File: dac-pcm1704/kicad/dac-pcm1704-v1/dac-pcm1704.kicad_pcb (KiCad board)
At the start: 4 copper layers, 76.2 x 53.3 mm, 81 parts, among them IC2 PCM1702P, IC3 PCM1704U, J10 GND, J11 +15VAIN, J12 GND, J13 -15VAIN, J15 A, J16 +5VIN, J17 GND, J18 GND, J2 Conn_02x07_Odd_Even, J3 +5VAIN, J6 OUT, J7 -5VAIN, J8 GND, J9 OUT, U1 OPA1612, U2 TC1185-1.8VCT713, U3 TC1185-3.3VCT713, U4 XC2C64A-xVQ44, U5 CM1293A−04SO, U6 OPA1612

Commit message: WIP
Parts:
- removed IC2: PCM1702P, Package_DIP:DIP-16_W7.62mm
- added IC4: PCM1704U, Package_SO:SO-20_5.3x12.6mm_P1.27mm, F.Cu at (149.3, 99.5)
- C11, C12, C20, C21, C26: moved to B.Cu
- C25: footprint Capacitor_Tantalum_SMD:CP_EIA-3216-18_Kemet-A_Pad1.58x1.35mm_HandSolder -> Capacitor_SMD:C_1206_3216Metric_Pad1.33x1.80mm_HandSolder; moved to B.Cu
- C27, C28, C30: footprint Capacitor_Tantalum_SMD:CP_EIA-3216-18_Kemet-A_Pad1.58x1.35mm_HandSolder -> Capacitor_SMD:C_1206_3216Metric_Pad1.33x1.80mm_HandSolder
- C35, C36: footprint Capacitor_Tantalum_SMD:CP_EIA-3528-21_Kemet-B_Pad1.50x2.35mm_HandSolder -> Capacitor_SMD:C_1206_3216Metric_Pad1.33x1.80mm_HandSolder
- moved C11 33.3 mm to (149.0, 73.9), turned to 180 degrees
- moved C12 33.2 mm to (149.0, 71.3), turned to 180 degrees
- moved C16 31.6 mm to (154.4, 86.0)
- moved C10 31.2 mm to (156.6, 80.2)
- moved C29 31.2 mm to (141.4, 72.5)
- moved C14 31.2 mm to (143.5, 77.0)
- moved C9 31.2 mm to (153.8, 83.3)
- moved IC3 31.2 mm to (149.3, 75.7)
- moved C18 31.2 mm to (141.4, 77.6)
- moved C15 31.2 mm to (143.5, 73.2)
- moved C13 30.9 mm to (153.8, 68.1), turned to 0 degrees
- moved C17 30.6 mm to (154.3, 65.9), turned to 180 degrees
- moved C25 12.4 mm to (150.4, 101.7), turned to -90 degrees
- moved C26 8.43 mm to (148.2, 101.2), turned to -90 degrees
- moved C20 8.42 mm to (148.7, 97.6), turned to 180 degrees
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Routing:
- net +5VA: track 20.1 -> 54.4 mm, vias 0 -> 1
- net -5VA: track 36.2 -> 58.9 mm
- net DATAOUTL: track 2.86 -> 16.9 mm, vias 1 -> 2
- net GND: track 17.1 -> 28.3 mm, vias 0 -> 4
- net Net-(IC4-IOUT): track 15.2 -> 4.62 mm, vias 1 -> 0
- net CLKOUTL: track 12.5 -> 17.0 mm, vias 1 -> 2
- net LEOUTL: track 21.8 -> 22.6 mm, vias 1 -> 2
- net Net-(IC4-SERV_DC): track 2.35 -> 2.46 mm, vias 0 -> 1
- net Net-(IC4-REF_DC): track 2.35 -> 2.46 mm, vias 0 -> 1

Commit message: WIP
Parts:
- C14, C18: moved to B.Cu
- moved C18 9.16 mm to (150.4, 76.3), turned to -90 degrees
- moved C14 4.81 mm to (148.2, 75.8), turned to -90 degrees
- moved C19 2.39 mm to (156.6, 101.5)
- moved C21 2.39 mm to (148.7, 92.7)
- moved C22 2.39 mm to (143.6, 96.2)
- moved C23 2.39 mm to (153.8, 104.7)
- moved C25 2.39 mm to (150.4, 99.3)
- moved C30 2.39 mm to (154.3, 86.9)
- moved C20 2.39 mm to (148.7, 95.2)
- moved C24 2.39 mm to (153.8, 89.5)
- moved C26 2.39 mm to (148.2, 98.8)
- moved C27 2.39 mm to (141.4, 96.8)
- moved IC4 2.39 mm to (149.3, 97.1)
- moved C28 1.98 mm to (154.4, 107.4)
- moved C17 1.88 mm to (154.3, 64.1)
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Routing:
- net +5VA: track 54.4 -> 38.3 mm, vias 1 -> 0
- net LEOUTL: track 22.6 -> 6.68 mm, vias 2 -> 1
- net GND: track 28.3 -> 17.1 mm, vias 4 -> 0
- net CLKOUTL: track 17.0 -> 7.43 mm, vias 2 -> 1
- net DATAOUTL: track 16.9 -> 8.03 mm, vias 2 -> 1
- net -5VA: track 58.9 -> 63.8 mm, vias 1 -> 2
- net Net-(IC4-SERV_DC): track 2.46 -> 0.00 mm, vias 1 -> 0
- net Net-(IC4-REF_DC): track 2.46 -> 0.00 mm, vias 1 -> 0
- net Net-(IC4-BPO_DC): track 2.24 -> 0.00 mm
- net unconnected-(IC4-NC-Pad8): track 0.00 -> 0.60 mm

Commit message: WIP
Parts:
- removed J15: A, kicad-snk:TE_CONN_RCPT_10POS_0.1_TIN_PCB
- added J4: TE MicroMatch, Connector_TE-Connectivity:TE_Micro-MaTch_1-215079-0_2x05_P1.27mm_Vertical, F.Cu at (112.8, 74.6)
- moved C27 1.22 mm to (140.2, 96.8)
- moved C29 0.91 mm to (140.2, 73.7)
- moved C15 0.91 mm to (142.6, 73.2)
- moved C22 0.91 mm to (142.6, 96.2)
- moved C11 0.10 mm to (148.7, 72.2)
- moved C12 0.05 mm to (148.7, 69.6)
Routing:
- net GND: track 17.1 -> 56.1 mm, vias 0 -> 4
- net -5VA: track 63.8 -> 101.1 mm, vias 2 -> 4
- net +5VA: track 38.3 -> 60.5 mm, vias 0 -> 4
- net Net-(IC3-SERV_DC): track 0.00 -> 2.54 mm, vias 0 -> 1
- net Net-(IC3-REF_DC): track 0.00 -> 2.51 mm, vias 0 -> 1
- net Net-(IC4-SERV_DC): track 0.00 -> 2.46 mm, vias 0 -> 1
- net Net-(IC4-REF_DC): track 0.00 -> 2.46 mm, vias 0 -> 1
- net Net-(IC4-BPO_DC): track 0.00 -> 2.24 mm
- net Net-(IC3-BPO_DC): track 0.00 -> 2.24 mm

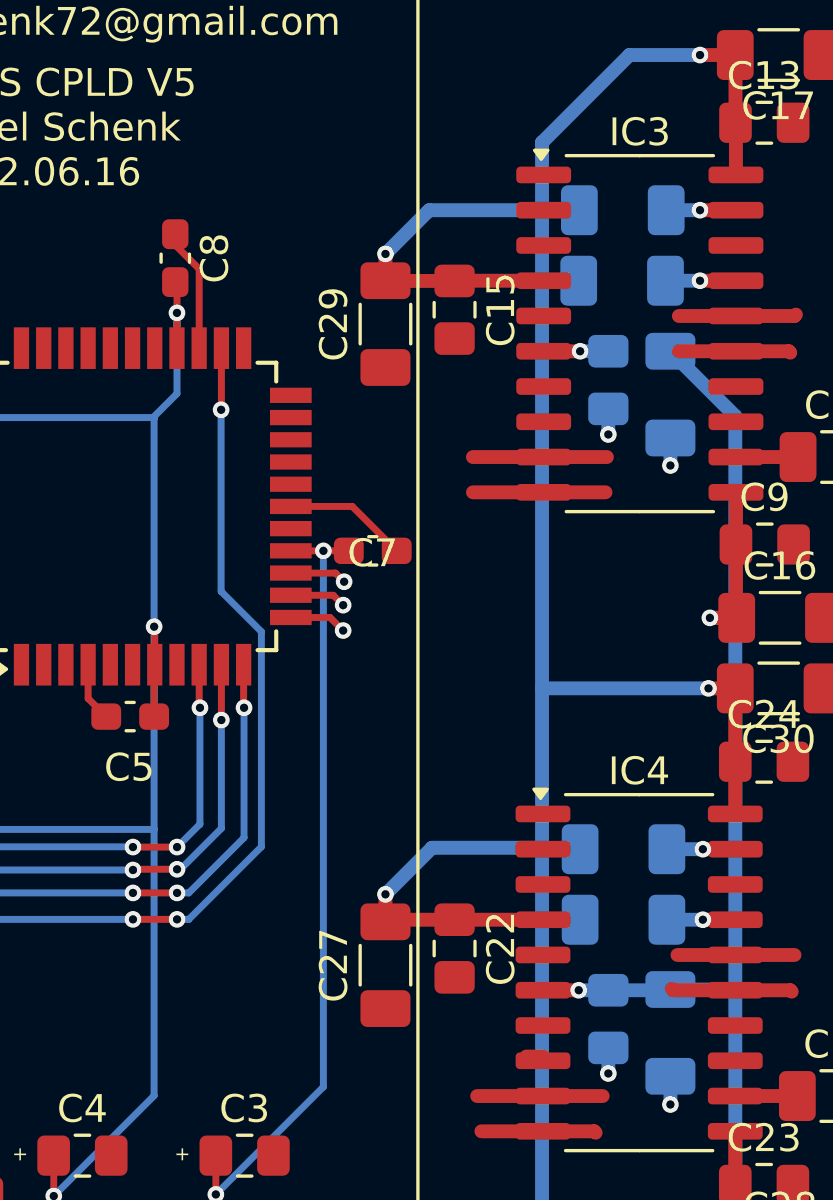
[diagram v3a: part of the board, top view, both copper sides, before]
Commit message: Update dac-pcm1704.kicad_pcb
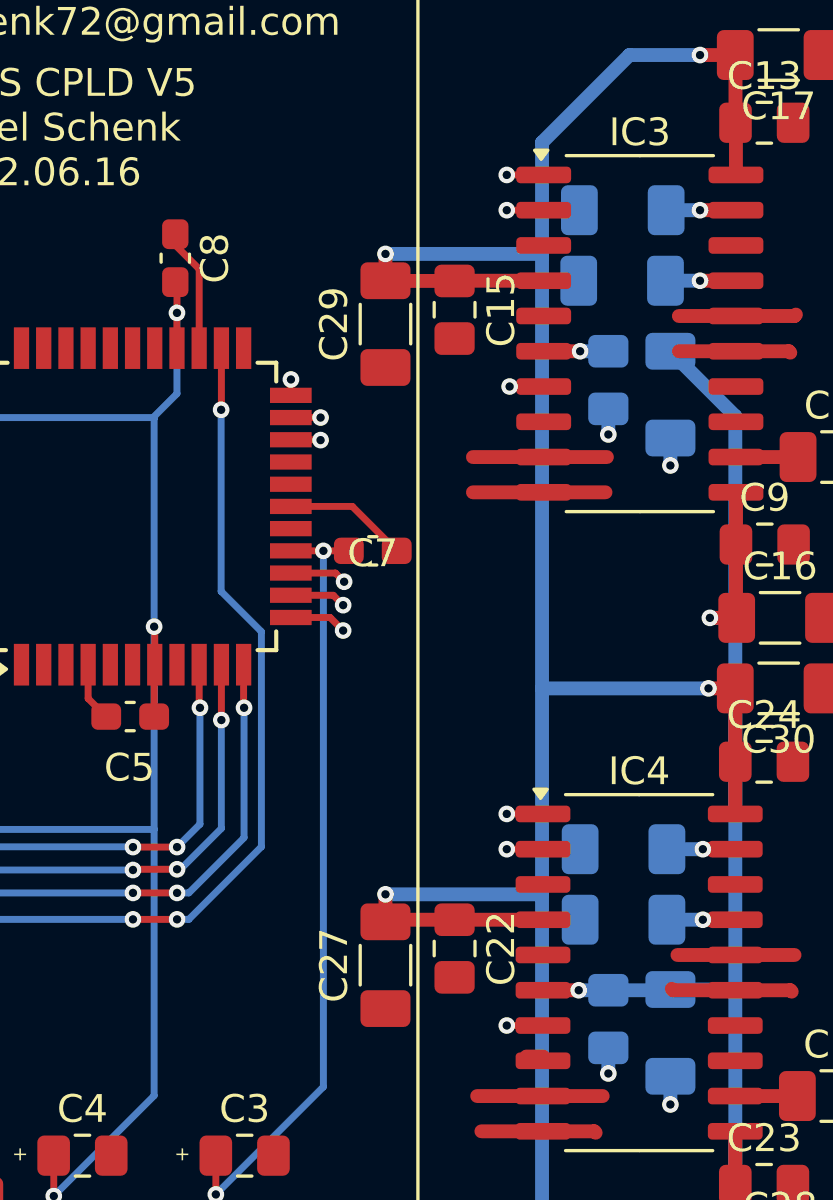
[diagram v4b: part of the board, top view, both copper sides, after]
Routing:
- net DATAOUTR: track 0.00 -> 12.7 mm, vias 0 -> 2
- net CLKOUTR: track 0.00 -> 12.6 mm, vias 0 -> 2
- net LEOUTR: track 0.00 -> 9.91 mm, vias 0 -> 2
- net DATAOUTL: track 8.03 -> 3.36 mm, vias 1 -> 2
- net CLKOUTL: track 7.43 -> 3.34 mm, vias 1 -> 2
- net LEOUTL: track 6.68 -> 3.38 mm, vias 1 -> 2
- net -5VA: track 101.1 -> 99.7 mm
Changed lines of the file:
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@@
+	)
+	(segment
+		(start 136.749 76.315)
+		(end 136.749 75.7474)
+		(width 0.25)
+		(layer "F.Cu")
+		(net 13)
+	)
+	(segment
+		(start 136.749 75.7474)
+		(end 136.7536 75.7428)
+		(width 0.25)
+		(layer "F.Cu")
+		(net 13)
+	)
+	(segment
+		(start 145.8552 68.3768)
+		(end 144.526 68.3768)
+		(width 0.25)
+		(layer "F.Cu")
+		(net 13)
+	)
+	(via
+		(at 144.526 68.3768)
+		(size 0.6)
+		(drill 0.3)
+		(layers "F.Cu" "B.Cu")
+		(net 13)
+	)
+	(via
+		(at 136.7536 75.7428)
+		(size 0.6)
+		(drill 0.3)
+		(layers "F.Cu" "B.Cu")
+		(net 13)
+	)
+	(segment
+		(start 144.526 68.3768)
+		(end 144.1196 68.3768)
+		(width 0.25)
+		(layer "In1.Cu")
+		(net 13)
+	)
+	(segment
+		(start 144.1196 68.3768)
+		(end 136.7536 75.7428)
+		(width 0.25)
+		(layer "In1.Cu")
+		(net 13)
 	)
 	(segment
@@
 	)
 	(segment
+		(start 145.8306 91.3892)
+		(end 144.526 91.3892)
+		(width 0.25)
+		(layer "F.Cu")
+		(net 14)
+	)
+	(segment
 		(start 138.355937 82.715)
 		(end 138.668128 83.027191)
@@
 	)
 	(via
+		(at 144.526 91.3892)
+		(size 0.6)
+		(drill 0.3)
+		(layers "F.Cu" "B.Cu")
+		(net 14)
+	)
+	(via
 		(at 138.668128 83.027191)
 		(size 0.6)
@@
 	)
 	(segment
-		(start 142.9004 87.252702)
-		(end 138.674889 83.027191)
+		(start 138.674889 83.027191)
+		(end 138.668128 83.027191)
 		(width 0.25)
 		(layer "In1.Cu")
@@
 	)
 	(segment
-		(start 138.674889 83.027191)
-		(end 138.668128 83.027191)
-		(width 0.25)
-		(layer "In1.Cu")
-		(net 14)
-	)
-	(segment
 		(start 152.7802 79.8068)
 		(end 152.7802 81.6864)
@@
 	)
 	(segment
-		(start 145.796 92.6084)
+		(start 145.796 94.2848)
 		(end 145.796 95.1484)
 		(width 0.5)
@@
 	)
 	(segment
-		(start 145.796 92.6084)
-		(end 141.8336 92.6084)
-		(width 0.5)
-		(layer "B.Cu")
-		(net 17)
-	)
-	(segment
 		(start 147.1676 95.1992)
 		(end 145.8468 95.1992)
@@
 	)
 	(segment
+		(start 145.796 69.596)
+		(end 145.796 71.3232)
+		(width 0.5)
+		(layer "B.Cu")
+		(net 17)
+	)
+	(segment
 		(start 145.796 95.1484)
 		(end 145.796 108.7755)
@@
 	)
 	(segment
-		(start 141.732 69.6468)
-		(end 140.1572 71.2216)
-		(width 0.5)
-		(layer "B.Cu")
-		(net 17)
-	)
-	(segment
 		(start 151.4856 64.0588)
 		(end 148.9456 64.0588)
@@
 	)
 	(segment
+		(start 140.1572 94.2848)
+		(end 145.796 94.2848)
+		(width 0.5)
+		(layer "B.Cu")
+		(net 17)
+	)
+	(segment
+		(start 145.6944 71.2216)
+		(end 145.796 71.3232)
+		(width 0.5)
+		(layer "B.Cu")
+		(net 17)
+	)
+	(segment
 		(start 147.1168 72.1868)
 		(end 145.796 72.1868)
@@
 	)
 	(segment
-		(start 145.796 69.596)
+		(start 145.796 92.6084)
+		(end 145.796 94.2848)
+		(width 0.5)
+		(layer "B.Cu")
+		(net 17)
+	)
+	(segment
+		(start 140.1572 71.2216)
+		(end 145.6944 71.2216)
+		(width 0.5)
+		(layer "B.Cu")
+		(net 17)
+	)
+	(segment
+		(start 145.796 71.3232)
 		(end 145.796 72.1868)
-		(width 0.5)
-		(layer "B.Cu")
-		(net 17)
-	)
-	(segment
-		(start 141.8336 92.6084)
-		(end 140.1572 94.2848)
-		(width 0.5)
-		(layer "B.Cu")
-		(net 17)
-	)
-	(segment
-		(start 145.8468 69.6468)
-		(end 141.732 69.6468)
 		(width 0.5)
 		(layer "B.Cu")
@@
 	)
 	(segment
+		(start 145.8552 75.9968)
+		(end 144.6276 75.9968)
+		(width 0.25)
+		(layer "F.Cu")
+		(net 22)
+	)
+	(segment
+		(start 136.749 77.915)
+		(end 137.8082 77.915)
+		(width 0.25)
+		(layer "F.Cu")
+		(net 22)
+	)
+	(segment
+		(start 137.8082 77.915)
+		(end 137.8204 77.9272)
+		(width 0.25)
+		(layer "F.Cu")
+		(net 22)
+	)
+	(via
+		(at 144.6276 75.9968)
+		(size 0.6)
+		(drill 0.3)
+		(layers "F.Cu" "B.Cu")
+		(net 22)
+	)
+	(via
+		(at 137.8204 77.9272)
+		(size 0.6)
+		(drill 0.3)
+		(layers "F.Cu" "B.Cu")
+		(net 22)
+	)
+	(segment
+		(start 137.8204 77.9272)
+		(end 139.192 77.9272)
+		(width 0.25)
+		(layer "In1.Cu")
+		(net 22)
+	)
+	(segment
+		(start 141.1224 75.9968)
+		(end 144.6276 75.9968)
+		(width 0.25)
+		(layer "In1.Cu")
+		(net 22)
+	)
+	(segment
+		(start 139.192 77.9272)
+		(end 141.1224 75.9968)
+		(width 0.25)
+		(layer "In1.Cu")
+		(net 22)
+	)
+	(segment
+		(start 137.8198 77.115)
+		(end 137.8204 77.1144)
+		(width 0.25)
+		(layer "F.Cu")
+		(net 23)
+	)
+	(segment
+		(start 136.749 77.115)
+		(end 137.8198 77.115)
+		(width 0.25)
+		(layer "F.Cu")
+		(net 23)
+	)
+	(segment
+		(start 145.8552 69.6468)
+		(end 144.526 69.6468)
+		(width 0.25)
+		(layer "F.Cu")
+		(net 23)
+	)
+	(via
+		(at 144.526 69.6468)
+		(size 0.6)
+		(drill 0.3)
+		(layers "F.Cu" "B.Cu")
+		(net 23)
+	)
+	(via
+		(at 137.8204 77.1144)
+		(size 0.6)
+		(drill 0.3)
+		(layers "F.Cu" "B.Cu")
+		(net 23)
+	)
+	(segment
+		(start 138.7856 75.3872)
+		(end 144.526 69.6468)
+		(width 0.25)
+		(layer "In1.Cu")
+		(net 23)
+	)
+	(segment
+		(start 137.8204 77.1144)
+		(end 138.7856 76.1492)
+		(width 0.25)
+		(layer "In1.Cu")
+		(net 23)
+	)
+	(segment
+		(start 138.7856 76.1492)
+		(end 138.7856 75.3872)
+		(width 0.25)
+		(layer "In1.Cu")
+		(net 23)
+	)
+	(segment
 		(start 136.749 84.315)
 		(end 138.163 84.315)
@@
 		(net 24)
 	)
+	(segment
+		(start 145.8306 99.0092)
+		(end 144.526 99.0092)
+		(width 0.25)
+		(layer "F.Cu")
+		(net 24)
+	)
 	(via
 		(at 138.6332 84.7852)
@@
 		(net 24)
 	)
-	(segment
-		(start 141.8844 88.0364)
-		(end 138.6332 84.7852)
-		(width 0.25)
-		(layer "In1.Cu")
+	(via
+		(at 144.526 99.0092)
+		(size 0.6)
+		(drill 0.3)
+		(layers "F.Cu" "B.Cu")
 		(net 24)
 	)
@@
 	)
 	(segment
+		(start 145.8306 92.6592)
+		(end 144.526 92.6592)
+		(width 0.25)
+		(layer "F.Cu")
+		(net 25)
+	)
+	(segment
 		(start 136.749 83.515)
 		(end 138.2774 83.515)
@@
 		(net 25)
 	)
-	(segment
-		(start 138.6332 83.8708)
-		(end 142.4494 87.687)
-		(width 0.25)
-		(layer "In1.Cu")
+	(via
+		(at 144.526 92.6592)
+		(size 0.6)
+		(drill 0.3)
+		(layers "F.Cu" "B.Cu")
 		(net 25)
 	)

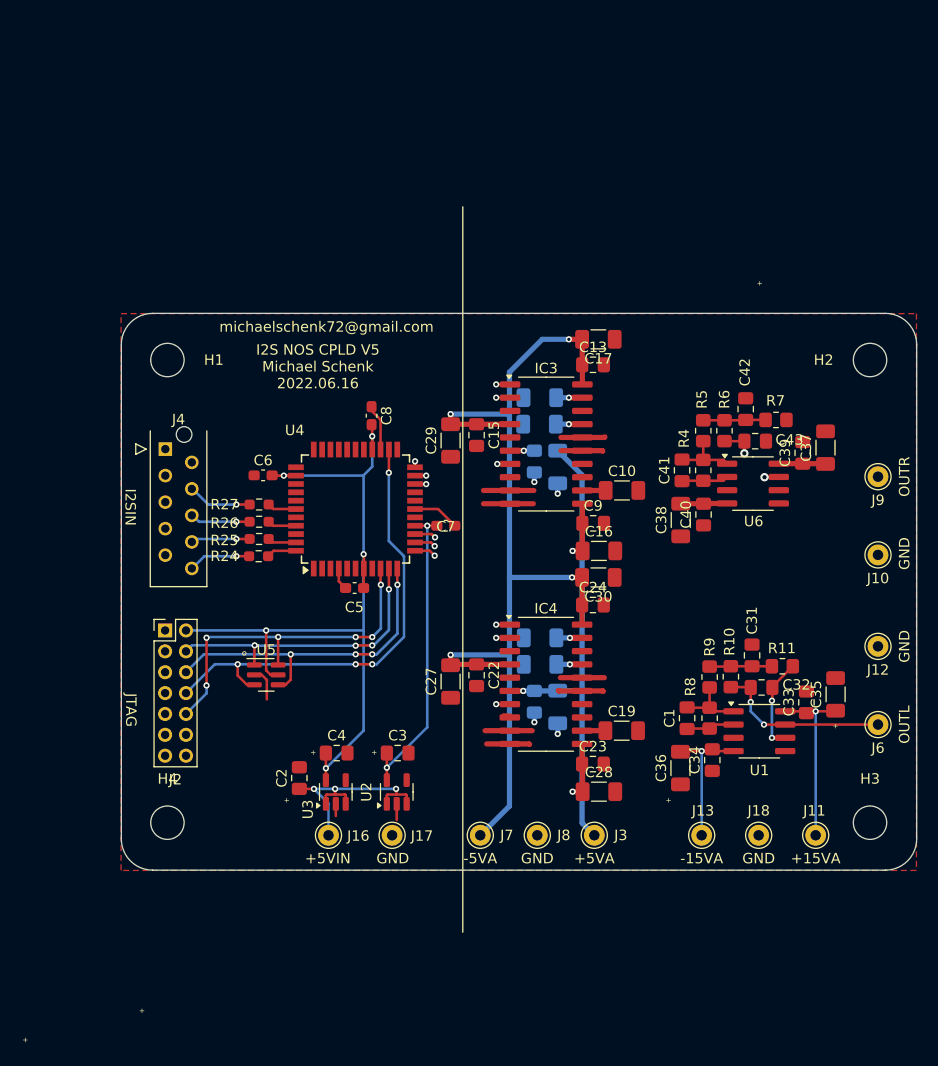
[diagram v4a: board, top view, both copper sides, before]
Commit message: Update dac-pcm1704.kicad_pcb
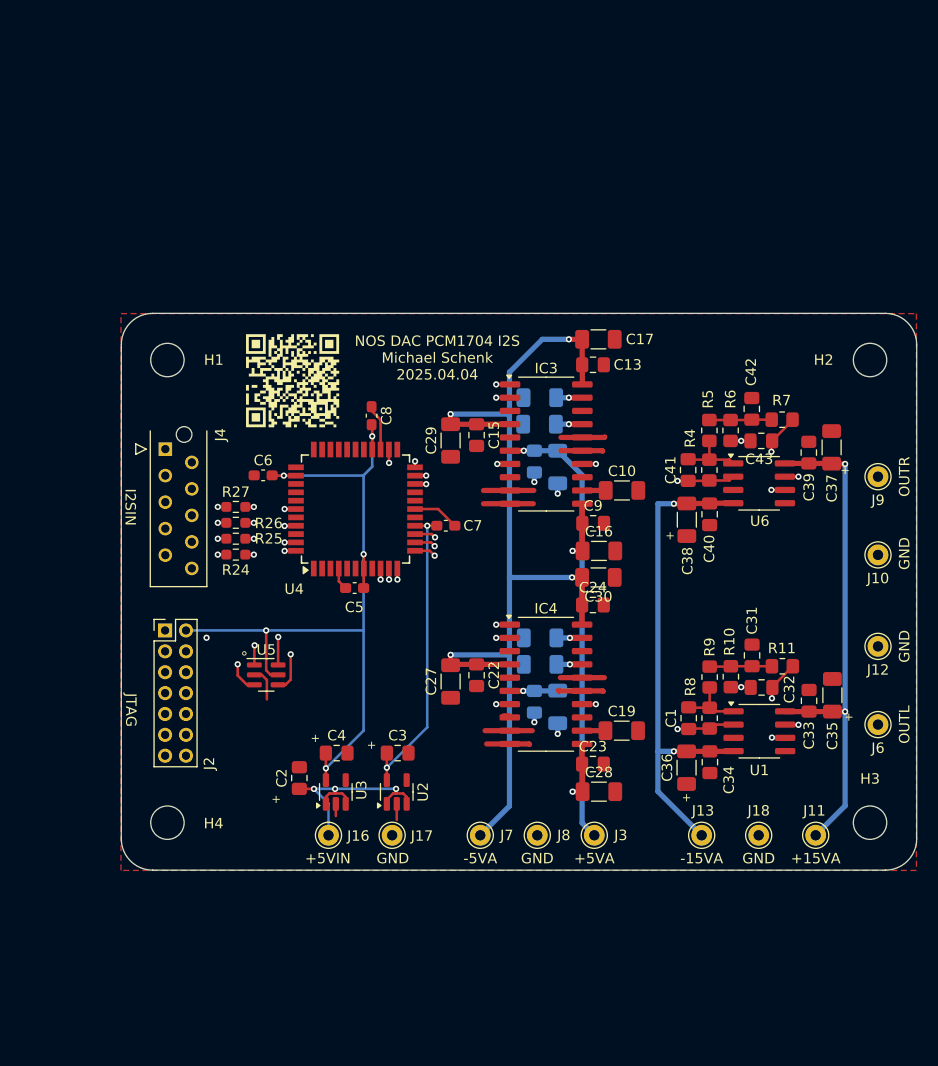
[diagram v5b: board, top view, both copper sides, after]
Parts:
- added G***: LOGO, LOGO, F.Cu at (125.0, 68.0)
- moved R27 2.24 mm to (119.6, 80.1)
- moved R26 2.23 mm to (119.6, 81.6)
- moved R25 2.23 mm to (119.6, 83.2)
- moved R24 2.19 mm to (119.6, 84.7)
- moved C36 0.59 mm to (162.8, 105.1)
- moved C39 0.58 mm to (174.5, 74.9)
- moved C40 0.58 mm to (165.0, 80.8)
- moved C41 0.58 mm to (162.9, 76.6)
- moved U6 0.58 mm to (169.7, 77.9)
- moved C37 0.58 mm to (176.7, 74.4)
- moved C38 0.58 mm to (162.8, 81.3)
- moved C43 0.58 mm to (169.9, 73.8)
- moved R6 0.58 mm to (167.0, 72.8)
- moved C42 0.58 mm to (169.0, 70.7)
- moved R4 0.58 mm to (164.9, 76.6)
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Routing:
- net -15V: track 17.6 -> 48.0 mm, vias 1 -> 2
- net +15V: track 21.2 -> 48.3 mm, vias 1 -> 2
- net LEOUTL: track 3.38 -> 20.0 mm
- net CLKOUTL: track 3.34 -> 14.6 mm
- net Net-(IC4-IOUT): track 4.62 -> 15.7 mm, vias 0 -> 2
- net Net-(IC3-IOUT): track 4.49 -> 15.3 mm, vias 0 -> 2
- net DATAOUTL: track 3.36 -> 14.1 mm
- net Net-(J9-Pin_1): track 7.54 -> 17.7 mm
- net Net-(U6B--): track 0.00 -> 8.86 mm, vias 0 -> 2
- net BCK: track 2.76 -> 5.00 mm, vias 0 -> 2
- net +5VA: track 60.5 -> 62.7 mm
- net LRCK: track 2.78 -> 4.99 mm, vias 0 -> 2
- net Net-(J4-Pin_6): track 5.74 -> 3.60 mm
- net DATAIN: track 2.80 -> 4.94 mm, vias 0 -> 2
- net MCLK: track 2.88 -> 5.00 mm, vias 0 -> 2
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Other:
- board text added: "NOS DAC PCM1704 I2S Michael Schenk 2025.04.04"
- board text removed: "I2S NOS CPLD V5 Michael Schenk 2022.06.16"
- board text removed: "michaelschenk72@gmail.com"

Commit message: Ready to order
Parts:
- U5: footprint Package_SO:SC-74-6_1.5x2.9mm_P0.95mm -> Package_TO_SOT_SMD:SC-74-6_1.55x2.9mm_P0.95mm
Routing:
- net GND: track 56.1 -> 65.9 mm
